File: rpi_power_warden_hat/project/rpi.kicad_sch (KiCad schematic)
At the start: 3 parts, among them J1 Raspberry_Pi_4

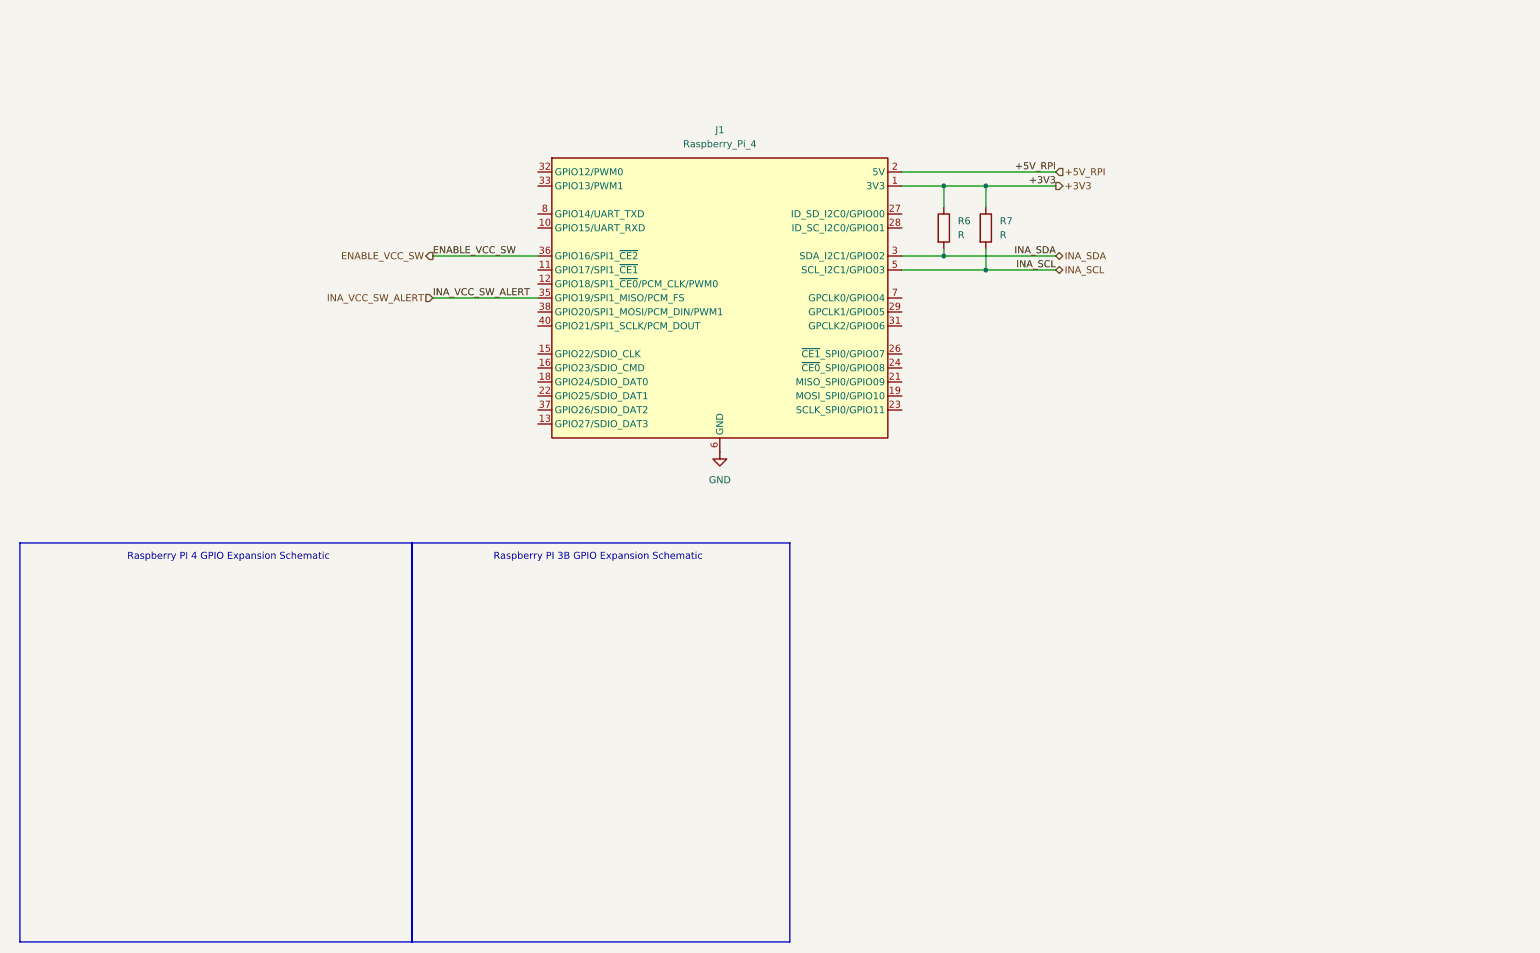
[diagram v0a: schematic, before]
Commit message: feat: put USB A receptacle to deliver power, have progress in INA260 and place test poitns
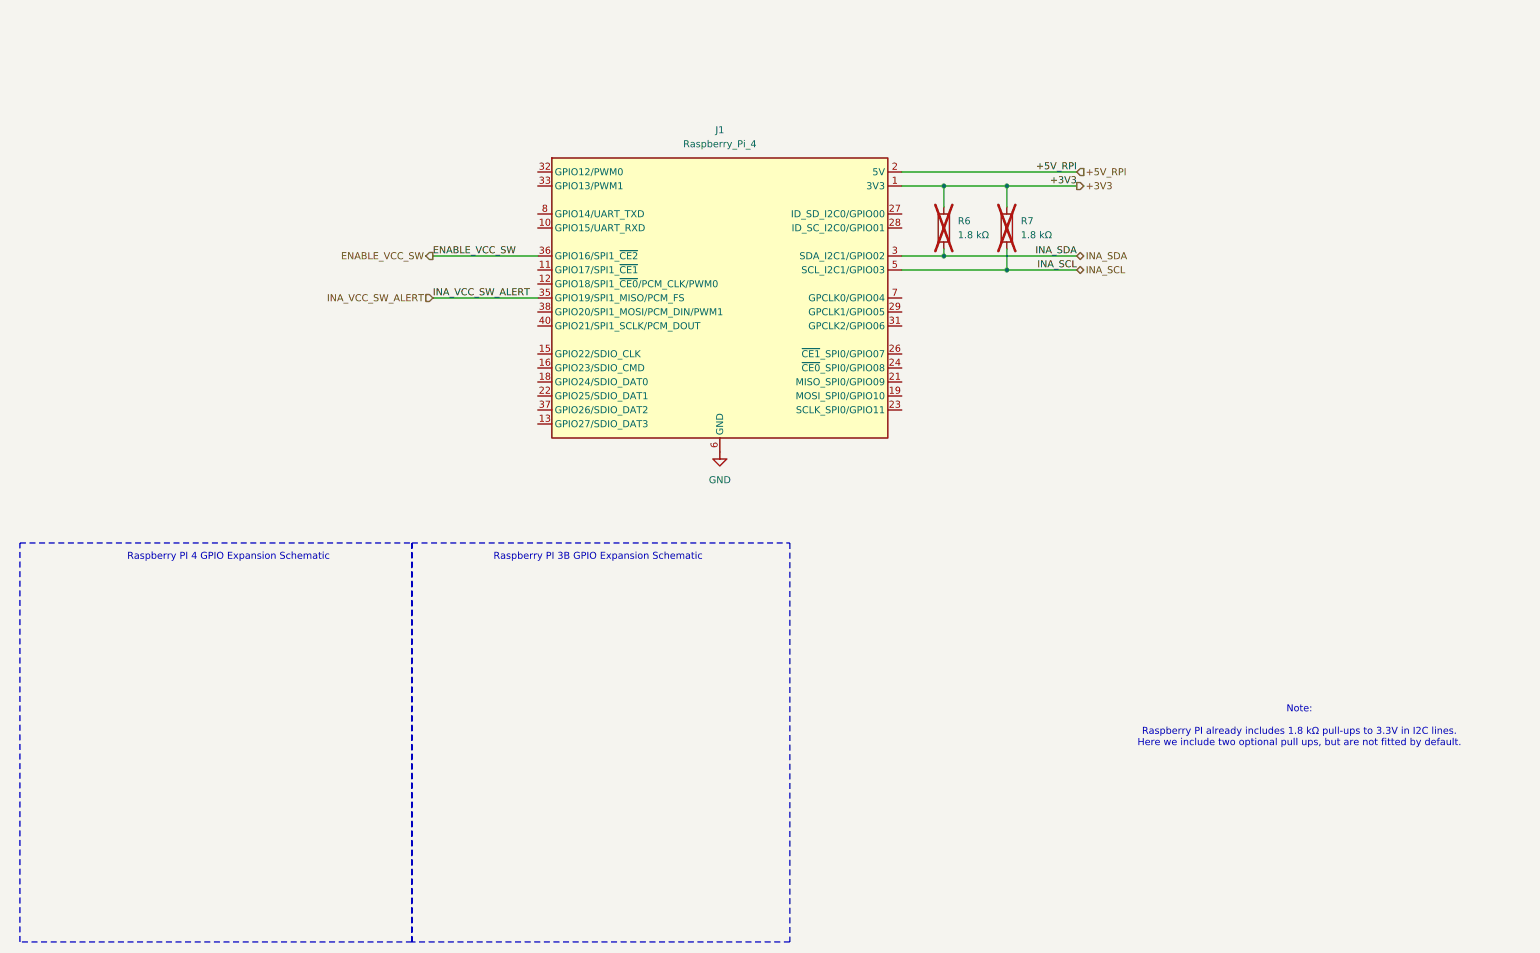
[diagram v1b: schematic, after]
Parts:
- R6, R7: value R -> 1.8 kΩ; footprint (none) -> Resistor_SMD:R_0603_1608Metric_Pad0.98x0.95mm_HandSolder; manufacturer (none) -> Panasonic Electronic Components; mpn (none) -> ERJ-3GEYJ182V; now not fitted; now left out of the parts list
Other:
- note added: "Note: Raspberry PI already includes 1.8 kΩ pull-ups to 3.3V in I2C lines. Here we include two optional pull ups, but are not fitted by default."
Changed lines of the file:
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@@
 	(paper "A4")
 	(junction
-		(at 190.5 57.15)
+		(at 194.31 57.15)
 		(diameter 0)
 		(color 0 0 0 0)
@@
 	)
 	(junction
-		(at 182.88 57.15)
+		(at 194.31 72.39)
 		(diameter 0)
 		(color 0 0 0 0)
 	)
 	(junction
-		(at 190.5 72.39)
+		(at 182.88 57.15)
 		(diameter 0)
 		(color 0 0 0 0)
@@
 	(wire
 		(pts
-			(xy 190.5 68.58) (xy 190.5 72.39)
+			(xy 194.31 68.58) (xy 194.31 72.39)
 		)
 		(stroke
@@
 	(wire
 		(pts
-			(xy 190.5 72.39) (xy 203.2 72.39)
+			(xy 175.26 54.61) (xy 207.01 54.61)
 		)
 		(stroke
@@
 	(wire
 		(pts
-			(xy 175.26 54.61) (xy 203.2 54.61)
+			(xy 175.26 57.15) (xy 182.88 57.15)
 		)
 		(stroke
@@
 	(wire
 		(pts
-			(xy 175.26 57.15) (xy 182.88 57.15)
+			(xy 194.31 57.15) (xy 207.01 57.15)
 		)
 		(stroke
@@
 	(wire
 		(pts
-			(xy 175.26 72.39) (xy 190.5 72.39)
+			(xy 175.26 72.39) (xy 194.31 72.39)
 		)
 		(stroke
@@
 	(wire
 		(pts
-			(xy 182.88 69.85) (xy 203.2 69.85)
+			(xy 182.88 69.85) (xy 207.01 69.85)
 		)
 		(stroke
@@
 	(wire
 		(pts
-			(xy 190.5 57.15) (xy 203.2 57.15)
+			(xy 182.88 57.15) (xy 194.31 57.15)
 		)
 		(stroke
@@
 	(wire
 		(pts
-			(xy 182.88 57.15) (xy 190.5 57.15)
+			(xy 175.26 69.85) (xy 182.88 69.85)
 		)
 		(stroke
@@
 	(wire
 		(pts
-			(xy 175.26 69.85) (xy 182.88 69.85)
+			(xy 90.17 69.85) (xy 109.22 69.85)
 		)
 		(stroke
@@
 	(wire
 		(pts
-			(xy 90.17 69.85) (xy 109.22 69.85)
+			(xy 194.31 57.15) (xy 194.31 60.96)
 		)
 		(stroke
@@
 	(wire
 		(pts
-			(xy 190.5 57.15) (xy 190.5 60.96)
+			(xy 194.31 72.39) (xy 207.01 72.39)
 		)
 		(stroke
@@
 		(stroke
 			(width 0)
-			(type default)
+			(type dash)
 		)
 		(fill
@@
 		(stroke
 			(width 0)
-			(type default)
+			(type dash)
 		)
 		(fill
@@
 		)
 	)
+	(text "Note:\n\nRaspberry PI already includes 1.8 kΩ pull-ups to 3.3V in I2C lines.\nHere we include two optional pull ups, but are not fitted by default."
+		(exclude_from_sim no)
+		(at 247.396 155.194 0)
+		(effects
+			(font
+				(size 1.27 1.27)
+			)
+		)
+	)
 	(text "Raspberry PI 3B GPIO Expansion Schematic\n"
 		(exclude_from_sim no)
@@
 	)
 	(label "INA_SCL"
-		(at 203.2 72.39 180)
+		(at 207.01 72.39 180)
 		(effects
 			(font
@@
 	)
 	(label "INA_SDA"
-		(at 203.2 69.85 180)
+		(at 207.01 69.85 180)
 		(effects
 			(font
@@
 	)
 	(label "+5V_RPI"
-		(at 203.2 54.61 180)
+		(at 207.01 54.61 180)
 		(effects
 			(font
@@
 	)
 	(label "+3V3"
-		(at 203.2 57.15 180)
+		(at 207.01 57.15 180)
 		(effects
 			(font
@@
 	(hierarchical_label "INA_SCL"
 		(shape bidirectional)
-		(at 203.2 72.39 0)
+		(at 207.01 72.39 0)
 		(effects
 			(font
@@
 	(hierarchical_label "INA_SDA"
 		(shape bidirectional)
-		(at 203.2 69.85 0)
+		(at 207.01 69.85 0)
 		(effects
 			(font
@@
 	(hierarchical_label "+3V3"
 		(shape output)
-		(at 203.2 57.15 0)
+		(at 207.01 57.15 0)
 		(effects
 			(font
@@
 	(hierarchical_label "+5V_RPI"
 		(shape input)
-		(at 203.2 54.61 0)
+		(at 207.01 54.61 0)
 		(effects
 			(font
@@
 	)
 	(symbol
+		(lib_id "Device:R")
+		(at 182.88 64.77 0)
+		(unit 1)
+		(exclude_from_sim no)
+		(in_bom no)
+		(on_board yes)
+		(dnp yes)
+		(fields_autoplaced yes)
+		(property "Reference" "R6"
+			(at 185.42 63.4999 0)
+			(effects
+				(font
+					(size 1.27 1.27)
+				)
+				(justify left)
+			)
+		)
+		(property "Value" "1.8 kΩ"
+			(at 185.42 66.0399 0)
+			(effects
+				(font
+					(size 1.27 1.27)
+				)
+				(justify left)
+			)
+		)
+		(property "Footprint" "Resistor_SMD:R_0603_1608Metric_Pad0.98x0.95mm_HandSolder"
+			(at 181.102 64.77 90)
+			(effects
+				(font
+					(size 1.27 1.27)
+				)
+				(hide yes)
+			)
+		)
+		(property "Datasheet" "~"
+			(at 182.88 64.77 0)
+			(effects
+				(font
+					(size 1.27 1.27)
+				)
+				(hide yes)
+			)
+		)
+		(property "Description" "RES SMD 1.8K OHM 5% 1/10W"
+			(at 182.88 64.77 0)
+			(effects
+				(font
+					(size 1.27 1.27)
+				)
+				(hide yes)
+			)
+		)
+		(property "mpn" "ERJ-3GEYJ182V"
+			(at 182.88 64.77 0)
+			(effects
+				(font
+					(size 1.27 1.27)
+				)
+				(hide yes)
+			)
+		)
+		(property "manufacturer" "Panasonic Electronic Components"
+			(at 182.88 64.77 0)
+			(effects
+				(font
+					(size 1.27 1.27)
+				)
+				(hide yes)
+			)
+		)
+		(pin "1"
+		)
+		(pin "2"
+		)
+		(instances
+			(project "rpi_power_warden_hat"
+				(path "/8692c5de-a943-41e8-8e29-f6c5e99cda34/5b5e45a1-b5e5-41dc-86e3-95314fe825a7"
+					(reference "R6")
+					(unit 1)
+				)
+			)
+		)
+	)
+	(symbol
 		(lib_id "Connector:Raspberry_Pi_4")
 		(at 142.24 77.47 0)
@@
 	(symbol
 		(lib_id "Device:R")
-		(at 190.5 64.77 0)
+		(at 194.31 64.77 0)
 		(unit 1)
 		(exclude_from_sim no)
-		(in_bom yes)
+		(in_bom no)
 		(on_board yes)
-		(dnp no)
+		(dnp yes)
 		(fields_autoplaced yes)
 		(property "Reference" "R7"
-			(at 193.04 63.4999 0)
+			(at 196.85 63.4999 0)
 			(effects
 				(font
@@
 			)
 		)
-		(property "Value" "R"
-			(at 193.04 66.0399 0)
+		(property "Value" "1.8 kΩ"
+			(at 196.85 66.0399 0)
 			(effects
 				(font
@@
 			)
 		)
-		(property "Footprint" ""
-			(at 188.722 64.77 90)
+		(property "Footprint" "Resistor_SMD:R_0603_1608Metric_Pad0.98x0.95mm_HandSolder"
+			(at 192.532 64.77 90)
 			(effects
 				(font
@@
 		)
 		(property "Datasheet" "~"
-			(at 190.5 64.77 0)
+			(at 194.31 64.77 0)
 			(effects
 				(font
@@
 			)
 		)
-		(property "Description" "Resistor"
-			(at 190.5 64.77 0)
+		(property "Description" "RES SMD 1.8K OHM 5% 1/10W"
+			(at 194.31 64.77 0)
 			(effects
 				(font
@@
 			)
 		)
-		(pin "1"
-		)
-		(pin "2"
-		)
-		(instances
-			(project "rpi_power_warden_hat"
-				(path "/8692c5de-a943-41e8-8e29-f6c5e99cda34/5b5e45a1-b5e5-41dc-86e3-95314fe825a7"
-					(reference "R7")
-					(unit 1)
-				)
-			)
-		)
-	)
-	(symbol
-		(lib_id "Device:R")
-		(at 182.88 64.77 0)
-		(unit 1)
-		(exclude_from_sim no)
-		(in_bom yes)
-		(on_board yes)
-		(dnp no)
-		(fields_autoplaced yes)
-		(property "Reference" "R6"
-			(at 185.42 63.4999 0)
-			(effects
-				(font
-					(size 1.27 1.27)
-				)
-				(justify left)
-			)
-		)
-		(property "Value" "R"
-			(at 185.42 66.0399 0)
-			(effects
-				(font
-					(size 1.27 1.27)
-				)
-				(justify left)
-			)
-		)
-		(property "Footprint" ""
-			(at 181.102 64.77 90)
-			(effects
-				(font
-					(size 1.27 1.27)
-				)
-				(hide yes)
-			)
-		)
-		(property "Datasheet" "~"
-			(at 182.88 64.77 0)
+		(property "mpn" "ERJ-3GEYJ182V"
+			(at 194.31 64.77 0)
 			(effects
 				(font
@@
 			)
 		)
-		(property "Description" "Resistor"
-			(at 182.88 64.77 0)
+		(property "manufacturer" "Panasonic Electronic Components"
+			(at 194.31 64.77 0)
 			(effects
 				(font
@@
 			(project "rpi_power_warden_hat"
 				(path "/8692c5de-a943-41e8-8e29-f6c5e99cda34/5b5e45a1-b5e5-41dc-86e3-95314fe825a7"
-					(reference "R6")
+					(reference "R7")
 					(unit 1)
 				)

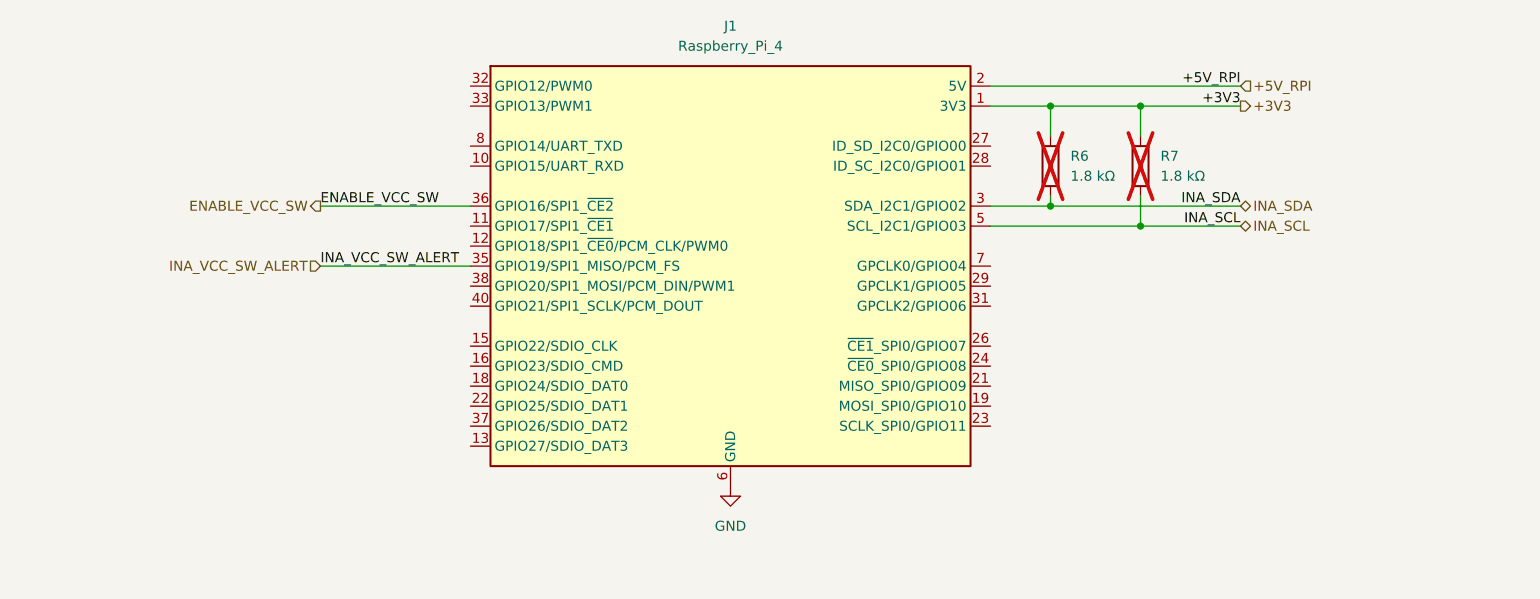
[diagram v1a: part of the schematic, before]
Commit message: add a switched vbat feature
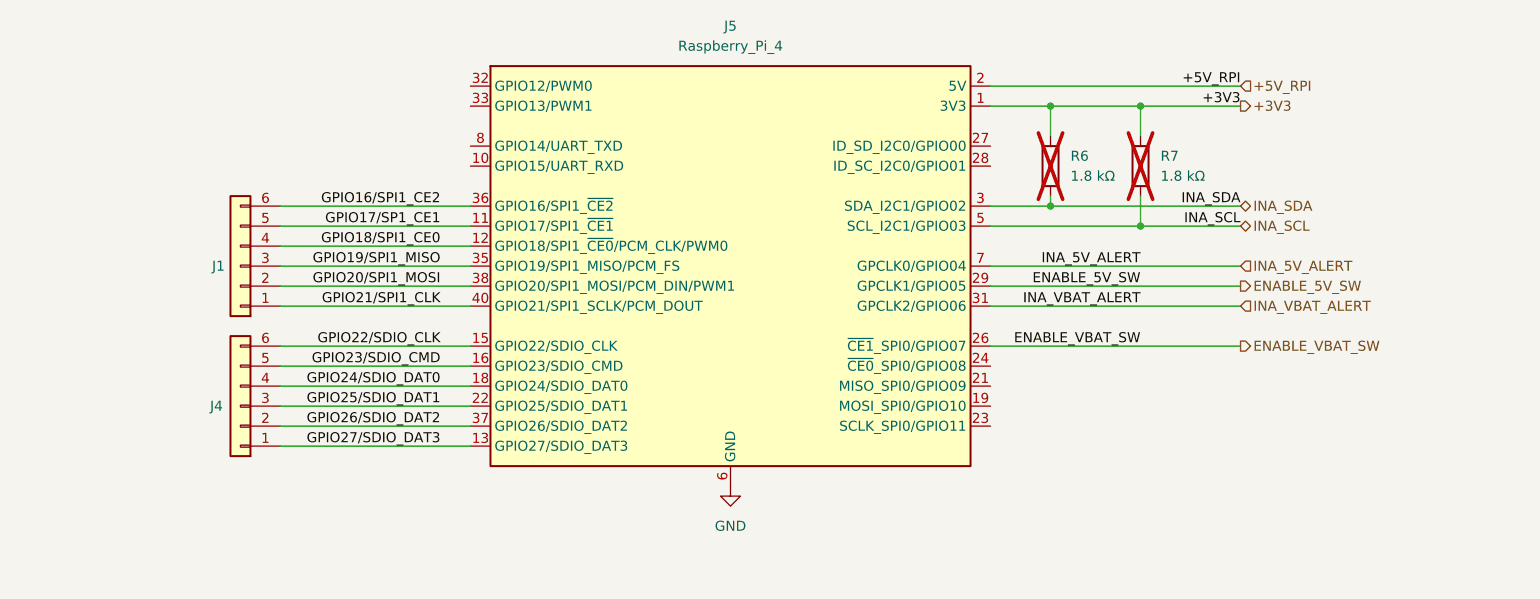
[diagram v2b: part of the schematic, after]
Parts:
- added J1, J4: Conn_01x06, symbol Connector_Generic:Conn_01x06
- renumbered J1 to J5
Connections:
- net GPIO17/SP1_CE1: now reaches J5.11 (GPIO17/SPI1_~{CE1})
- net GPIO17/SP1_CE1: now also J1.5 (Pin_5)
- net GPIO18/SPI1_CE0: now reaches J5.12 (GPIO18/SPI1_~{CE0}/PCM_CLK/PWM0)
- net GPIO18/SPI1_CE0: now also J1.4 (Pin_4)
- net GPIO27/SDIO_DAT3: now reaches J5.13 (GPIO27/SDIO_DAT3)
- net GPIO27/SDIO_DAT3: now also J4.1 (Pin_1)
- net GPIO22/SDIO_CLK: now reaches J5.15 (GPIO22/SDIO_CLK)
- net GPIO22/SDIO_CLK: now also J4.6 (Pin_6)
- net GPIO23/SDIO_CMD: now reaches J5.16 (GPIO23/SDIO_CMD)
- net GPIO23/SDIO_CMD: now also J4.5 (Pin_5)
- net GPIO24/SDIO_DAT0: now reaches J5.18 (GPIO24/SDIO_DAT0)
- net GPIO24/SDIO_DAT0: now also J4.4 (Pin_4)
- net GPIO25/SDIO_DAT1: now reaches J5.22 (GPIO25/SDIO_DAT1)
- net GPIO25/SDIO_DAT1: now also J4.3 (Pin_3)
- net ENABLE_VBAT_SW: now reaches J5.26 (~{CE1}_SPI0/GPIO07)
- net ENABLE_5V_SW: now reaches J5.29 (GPCLK1/GPIO05)
- net INA_VBAT_ALERT: now reaches J5.31 (GPCLK2/GPIO06)
- net GPIO26/SDIO_DAT2: now reaches J5.37 (GPIO26/SDIO_DAT2)
- net GPIO26/SDIO_DAT2: now also J4.2 (Pin_2)
- net GPIO20/SPI1_MOSI: now reaches J5.38 (GPIO20/SPI1_MOSI/PCM_DIN/PWM1)
- net GPIO20/SPI1_MOSI: now also J1.2 (Pin_2)
- net GPIO21/SPI1_CLK: now reaches J5.40 (GPIO21/SPI1_SCLK/PCM_DOUT)
- net GPIO21/SPI1_CLK: now also J1.1 (Pin_1)
- net INA_5V_ALERT: now reaches J5.7 (GPCLK0/GPIO04)
- net ENABLE_VCC_SW renamed GPIO16/SPI1_CE2
- net GPIO16/SPI1_CE2: now also J1.6 (Pin_6)
- net INA_VCC_SW_ALERT renamed GPIO19/SPI1_MISO
- net GPIO19/SPI1_MISO: now also J1.3 (Pin_3)
